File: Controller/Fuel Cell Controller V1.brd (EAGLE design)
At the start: 160 x 100 mm, 101 parts, among them IC1 4081D, M1 MOSFETBOARD, T1 TEENSY_3.1_ALL_PINS, U1 SN74ALS153D, U2 MAX3221CPWR, U3 ATMEGA328P_TQFP, U4 ATMEGA328P_TQFP, U5 MAX3221CPWR, U6 SN74HC4040D

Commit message: main board routed
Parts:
- added C19: 0.1uF, adafruit:C0603
- added C20: 10uF, adafruit:C0603
- added FRAME7: FRAME-LETTERNO_PACKAGE, SparkFun-Aesthetics:DUMMY
- added ISP3: AVRISP-BOX, adafruit:AVRISP-BOX
- added LED10, LED11, LED12, LED9: (no value), adafruit:CHIPLED_0805
- added R30, R31, R32, R33, R34: 100, adafruit:R0603
- C10, C2: value (none) -> 10uF
- C11, C12, C7, C8: value (none) -> 22pF
- C5, C9: value (none) -> 0.1uF
- R14, R9: value (none) -> 10k
- R22: value (none) -> 10k; device SparkFun-Resistors:0805 -> adafruit:R0603
- R23, R24, R25, R26, R27, R28, R29: value (none) -> 100; device SparkFun-Resistors:0805 -> adafruit:R0603
- U6: value SN74HC4040D -> ATMEGA328P_TQFP; device Texas Instruments_By_element14_Batch_1:SOIC127P600X175-16N -> SparkFun-DigitalIC:TQFP32-08
- moved R19 68.9 mm to (69.1, 18.7)
- moved R18 65.2 mm to (66.2, 18.6), turned to 90 degrees
- moved LED1 61.9 mm to (104.1, 87.0)
- moved LED2 57.4 mm to (102.2, 87.0)
- moved R20 55.3 mm to (50.3, 86.2), turned to 90 degrees
- moved LED3 52.9 mm to (100.3, 87.0)
- moved LED4 48.6 mm to (98.4, 87.0)
- moved R22 47.6 mm to (103.8, 62.5), turned to 180 degrees
- moved R23 36.1 mm to (91.4, 67.3), turned to 180 degrees
- moved R24 31.4 mm to (91.4, 69.5), turned to 180 degrees
- moved R25 27.6 mm to (87.0, 73.0), flipped to the bottom, turned to 270 degrees
- moved R29 22.9 mm to (84.1, 73.3)
- moved R13 17.2 mm to (34.5, 30.2), turned to 90 degrees
- moved R28 16.9 mm to (93.3, 66.0), flipped to the bottom, turned to 0 degrees
- moved U6 14.8 mm to (84.5, 65.4)
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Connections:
- removed net 5V: ETH2.P$5
- removed net GND1: ISP1.6
- removed net LED_CLK: T1.13, U6.10
- removed net N$17: R18.2, R19.2
- removed net V+: U2.16, U5.16
- removed net VCC: ISP1.2, ISP2.2
- new net ATMEG3_RESET: ISP3.5, R22.1, U6.29
- new net MISO3: ISP3.1, U6.16
- new net MOSI3: ISP3.4, U6.15
- new net N$39: LED7.A, R29.1
- new net N$40: LED6.A, R28.1
- new net N$41: LED5.A, R27.1
- new net N$42: LED4.A, R26.1
- new net N$43: LED3.A, R25.1
- new net N$44: LED2.A, R24.1
- new net N$45: LED1.A, R23.1
- new net N$46: ETH5.P$3, R19.1
- new net SCK3: ISP3.3, U6.17
- new net THIS_IS_NOT_CONNECTED_1: ISP1.2
- new net THIS_IS_NOT_CONNECTED_2: ISP2.2
- new net THIS_IS_NOT_CONNECTED_3: ISP3.2
- net +3.3V: now also C19.1, C20.1, R22.2, U2.16, U5.16, U6.18, U6.20, U6.4, U6.6; no longer CAN1.VIN, U6.16
- net FC5: now also ETH2.P$5
- net FCPRES: now also R18.2, R19.2, T1.A11; no longer ETH5.P$3, R19.1, T1.23/A9
- net GND: now also C19.2, C20.2, ISP1.6, ISP3.6, LED10.C, LED11.C, LED12.C, LED9.C, U6.21, U6.3, U6.5; no longer U6.8
- net N$16: now also R23.2, U6.23; no longer LED1.A, R22.1
- net N$18: now also R24.2, U6.24; no longer LED2.A, R23.1
- net N$19: now also R25.2, U6.25; no longer LED3.A, R24.1
- net N$20: now also R26.2, U6.26; no longer LED4.A, R25.1
- net N$21: now also R27.2, U6.19; no longer R22.2, U6.9
- net N$22: now also R28.2, U6.22; no longer R23.2, U6.7
- net N$28: now also R29.2, U6.30; no longer R24.2, U6.6
- net N$29: now also R30.2, U6.31; no longer R25.2, U6.5
- net N$30: now also R31.2, U6.32; no longer R26.2, U6.3
- net N$31: now also R32.2, U6.1; no longer R27.2, U6.2
- net N$32: now also R33.2, U6.2; no longer R28.2, U6.4
- net N$33: now also R34.2, U6.9; no longer R29.2, U6.13
- net N$34: now also LED12.A, R34.1; no longer U6.11, U6.12
- net N$35: now also LED11.A, R33.1; no longer LED5.A, R26.1
- net N$36: now also LED10.A, R32.1; no longer LED6.A, R27.1
- net N$37: now also LED9.A, R31.1; no longer LED7.A, R28.1
- net N$38: now also R30.1; no longer R29.1
- net SCL: now also U6.28
- net SDA: now also U6.27
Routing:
- net FC5: track 0.00 -> 361.8 mm, vias 0 -> 12
- net +3.3V: track 0.00 -> 255.9 mm, vias 0 -> 17
- net SDA: track 0.00 -> 242.7 mm, vias 0 -> 9
- net SCL: track 0.00 -> 237.0 mm, vias 0 -> 5
- net AUX12: track 0.00 -> 182.5 mm, vias 0 -> 4
- net FC12: track 0.00 -> 172.7 mm, vias 0 -> 3
- net H2_OK: track 0.00 -> 154.0 mm, vias 0 -> 8
- net FCPRES: track 0.00 -> 148.0 mm, vias 0 -> 3
- net RX1: track 0.00 -> 129.4 mm, vias 0 -> 3
- net TX1: track 0.00 -> 123.7 mm, vias 0 -> 3
- net AUX5: track 0.00 -> 116.2 mm
- net EXTRA_SIG: track 0.00 -> 110.8 mm, vias 0 -> 7
- net TX3: track 0.00 -> 82.6 mm, vias 0 -> 1
- net SUPPLY_V: track 0.00 -> 78.0 mm, vias 0 -> 4
- net CAPVOLT: track 0.00 -> 77.2 mm, vias 0 -> 5
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- added copper zone on layer 1, net FC12

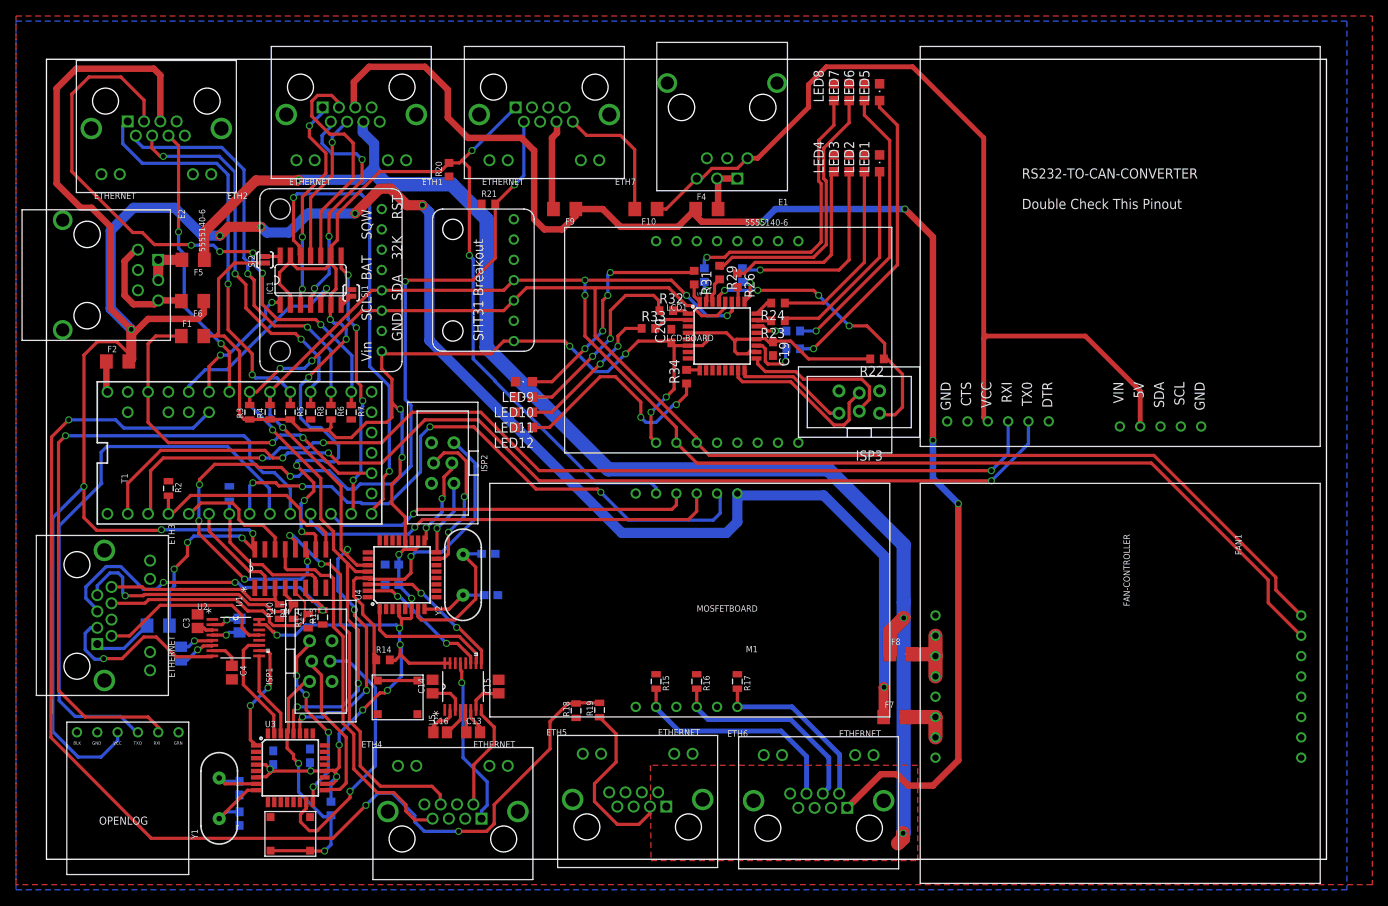
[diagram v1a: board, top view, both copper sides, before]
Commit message: added ground vias, making silk screen nice, starting documentation
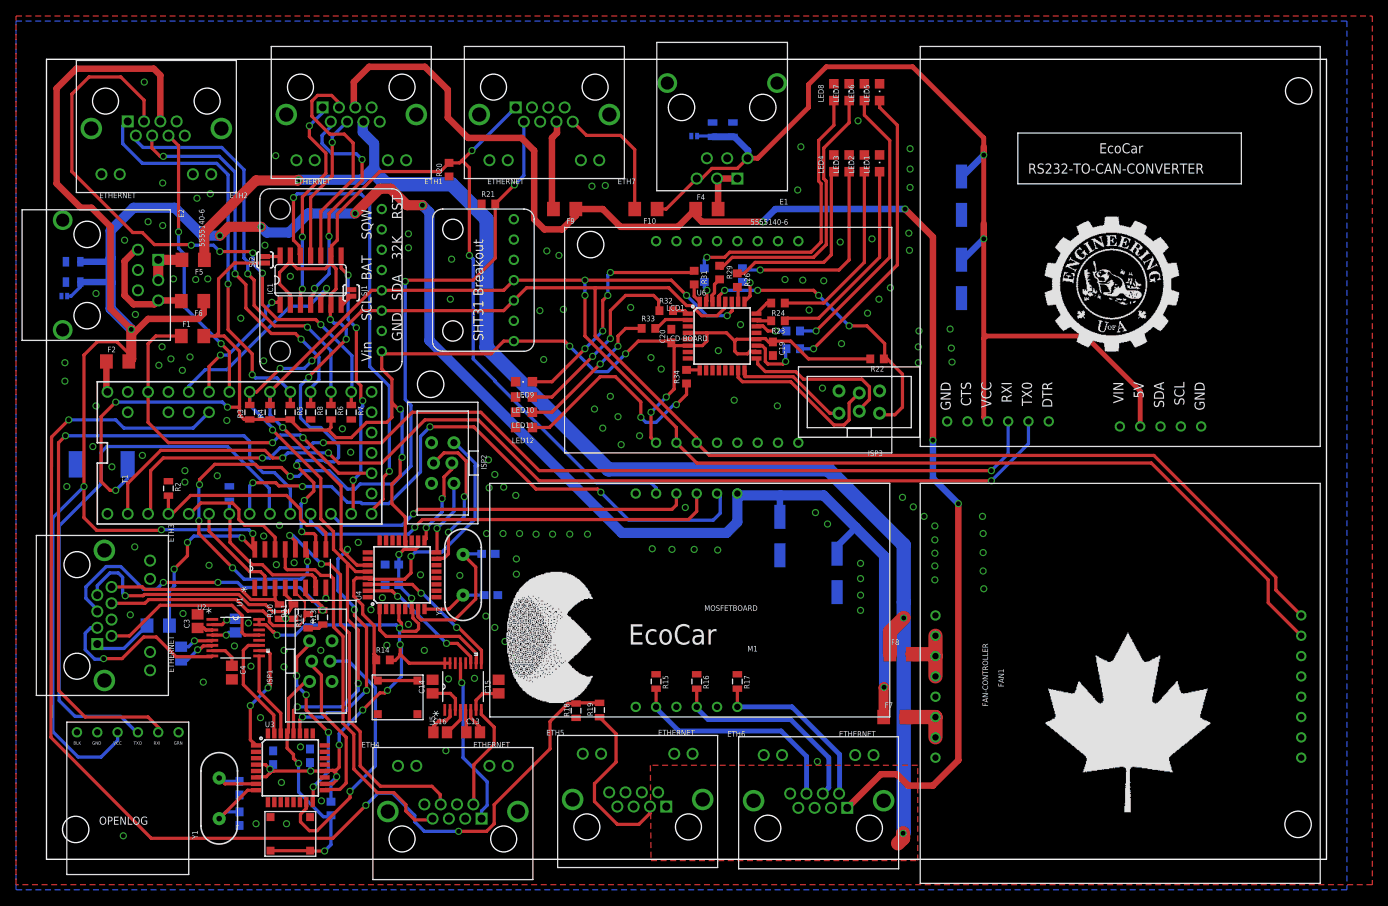
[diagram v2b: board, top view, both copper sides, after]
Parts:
- added C17, C18, C21, C25: 100uF, SparkFun-Capacitors:PANASONIC_D
- added C22, C23, C24, C26: 10uF, SparkFun-Capacitors-extra:0805
- added D1: SMBJ3V3(digikey), bt_diode:DO-214AB
- added D2, D3: TPD1E05U06DPYR, TPD1E05U06DPYR:2-XDFN
- added STANDOFF1, STANDOFF2, STANDOFF3, STANDOFF4, STANDOFF5: STAND-OFF, SparkFun-Electromechanical:STAND-OFF
- added U$1: TRUMP, trump:TRUMP
- moved C6 0.48 mm to (23.7, 29.2)
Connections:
- net +3.3V: now also D1.C
- net AUX5: now also C17.+, C21.+, C22.1, C23.1, D3.P$1
- net FC5: now also C18.+, C24.1, C25.+, C26.1, D2.P$1
- net GND: now also C17.-, C18.-, C21.-, C22.2, C23.2, C24.2, C25.-, C26.2, D1.A, D2.P$2, D3.P$2
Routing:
- net +3.3V: track 255.9 -> 291.9 mm, vias 17 -> 20
- net AUX5: track 116.2 -> 134.6 mm, vias 0 -> 2
- net FC5: track 361.8 -> 379.3 mm
- net GND: track 0.00 -> 2.84 mm, vias 0 -> 163

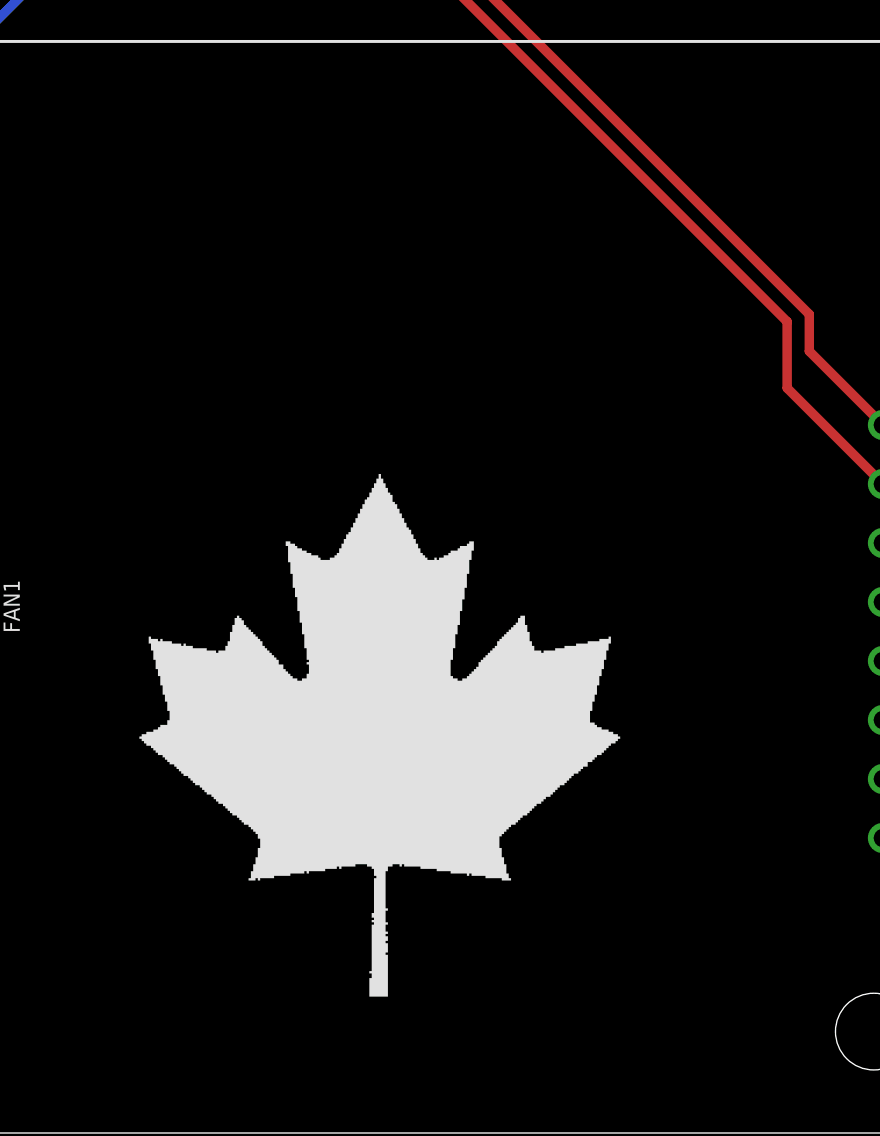
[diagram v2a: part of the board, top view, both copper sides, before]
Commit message: updated caps on fcc rs232 driver
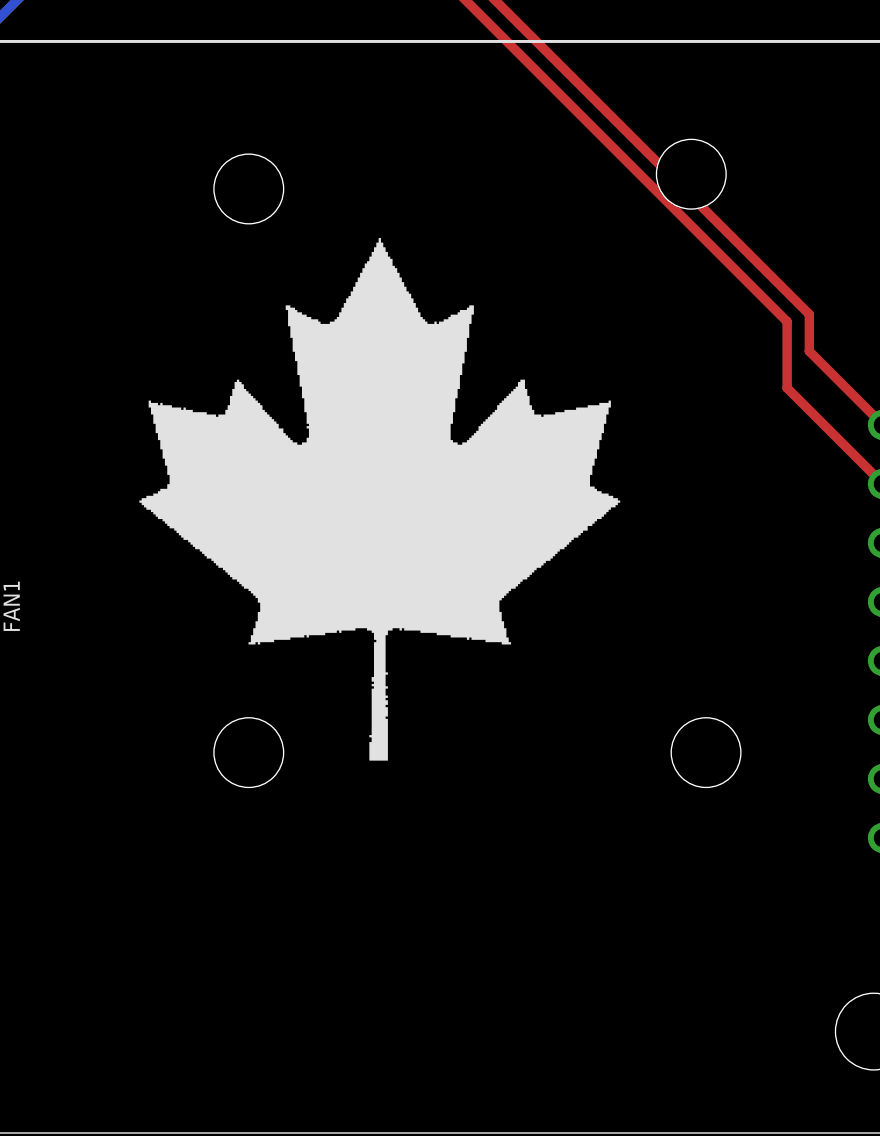
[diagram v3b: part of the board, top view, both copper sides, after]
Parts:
- C1, C13, C14, C15, C3, C4: value 0.33uF/12V -> 0.1uF/12V
- C16, C6: value 0.047uF/12V -> 0.1uF/12V
- moved U$1 48.2 mm to (148.1, 64.8)
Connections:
- removed net AGND: T1.AGND
- net GND: now also T1.AGND
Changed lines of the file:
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@@
 <attribute name="VALUE" x="17.96415" y="22.418675" size="0.7" layer="27" ratio="15" rot="SR0"/>
 </element>
-<element name="C6" library="E-P-008-R1.2" package="C0805" value="0.047uF/12V" x="23.65375" y="29.21" smashed="yes" rot="MR270">
+<element name="C6" library="E-P-008-R1.2" package="C0805" value="0.1uF/12V" x="23.65375" y="29.21" smashed="yes" rot="MR270">
 <attribute name="NAME" x="22.63775" y="30.099" size="0.7" layer="26" ratio="15" rot="MR270"/>
 <attribute name="VALUE" x="25.93975" y="30.099" size="0.7" layer="28" ratio="15" rot="MR270"/>
 </element>
-<element name="C1" library="E-P-008-R1.2" package="C0805" value="0.33uF/12V" x="16.8275" y="25.7175" smashed="yes" rot="MR270">
+<element name="C1" library="E-P-008-R1.2" package="C0805" value="0.1uF/12V" x="16.8275" y="25.7175" smashed="yes" rot="MR270">
 <attribute name="NAME" x="15.8115" y="26.6065" size="0.7" layer="26" ratio="15" rot="MR270"/>
 <attribute name="VALUE" x="19.1135" y="26.6065" size="0.7" layer="28" ratio="15" rot="MR270"/>
 </element>
-<element name="C3" library="E-P-008-R1.2" package="C0805" value="0.33uF/12V" x="18.89125" y="29.765625" smashed="yes" rot="R90">
+<element name="C3" library="E-P-008-R1.2" package="C0805" value="0.1uF/12V" x="18.89125" y="29.765625" smashed="yes" rot="R90">
 <attribute name="NAME" x="17.87525" y="28.876625" size="0.7" layer="25" ratio="15" rot="R90"/>
 <attribute name="VALUE" x="21.17725" y="28.876625" size="0.7" layer="27" ratio="15" rot="R90"/>
 </element>
-<element name="C4" library="E-P-008-R1.2" package="C0805" value="0.33uF/12V" x="23.1775" y="23.33625" smashed="yes" rot="R270">
+<element name="C4" library="E-P-008-R1.2" package="C0805" value="0.1uF/12V" x="23.1775" y="23.33625" smashed="yes" rot="R270">
 <attribute name="NAME" x="24.1935" y="24.22525" size="0.7" layer="25" ratio="15" rot="R270"/>
 <attribute name="VALUE" x="20.8915" y="24.22525" size="0.7" layer="27" ratio="15" rot="R270"/>
@@
 <attribute name="VALUE" x="57.3532" y="15.9004" size="0.7" layer="27" ratio="15" rot="SR90"/>
 </element>
-<element name="C16" library="E-P-008-R1.2" package="C0805" value="0.047uF/12V" x="49.2125" y="15.875" smashed="yes">
+<element name="C16" library="E-P-008-R1.2" package="C0805" value="0.1uF/12V" x="49.2125" y="15.875" smashed="yes">
 <attribute name="NAME" x="48.3235" y="16.891" size="0.7" layer="25" ratio="15"/>
 <attribute name="VALUE" x="48.3235" y="13.589" size="0.7" layer="27" ratio="15"/>
 </element>
-<element name="C13" library="E-P-008-R1.2" package="C0805" value="0.33uF/12V" x="53.34" y="15.875" smashed="yes">
+<element name="C13" library="E-P-008-R1.2" package="C0805" value="0.1uF/12V" x="53.34" y="15.875" smashed="yes">
 <attribute name="NAME" x="52.451" y="16.891" size="0.7" layer="25" ratio="15"/>
 <attribute name="VALUE" x="52.451" y="13.589" size="0.7" layer="27" ratio="15"/>
 </element>
-<element name="C14" library="E-P-008-R1.2" package="C0805" value="0.33uF/12V" x="48.26" y="21.59" smashed="yes" rot="R90">
+<element name="C14" library="E-P-008-R1.2" package="C0805" value="0.1uF/12V" x="48.26" y="21.59" smashed="yes" rot="R90">
 <attribute name="NAME" x="47.244" y="20.701" size="0.7" layer="25" ratio="15" rot="R90"/>
 <attribute name="VALUE" x="50.546" y="20.701" size="0.7" layer="27" ratio="15" rot="R90"/>
 </element>
-<element name="C15" library="E-P-008-R1.2" package="C0805" value="0.33uF/12V" x="56.515" y="21.59" smashed="yes" rot="R90">
+<element name="C15" library="E-P-008-R1.2" package="C0805" value="0.1uF/12V" x="56.515" y="21.59" smashed="yes" rot="R90">
 <attribute name="NAME" x="55.499" y="20.701" size="0.7" layer="25" ratio="15" rot="R90"/>
 <attribute name="VALUE" x="58.801" y="20.701" size="0.7" layer="27" ratio="15" rot="R90"/>
@@
 <attribute name="VALUE" x="80.0735" y="91.424125" size="0.7" layer="22" ratio="15" rot="MR180"/>
 </element>
-<element name="U$1" library="trump" package="TRUMP" value="TRUMP" x="145.494375" y="16.748125" rot="MR0"/>
+<element name="U$1" library="trump" package="TRUMP" value="TRUMP" x="148.11375" y="64.849375" rot="MR0"/>
 </elements>
 <signals>
@@
 <contactref element="D2" pad="P$2"/>
 <contactref element="D3" pad="P$2"/>
+<contactref element="T1" pad="AGND"/>
 </signal>
 <signal name="RX1">
@@
 <wire x1="92.6075" y1="67.6275" x2="92.29" y2="67.31" width="0.4064" layer="1"/>
 </signal>
-<signal name="AGND">
-<contactref element="T1" pad="AGND"/>
-</signal>
 <signal name="AREF">
